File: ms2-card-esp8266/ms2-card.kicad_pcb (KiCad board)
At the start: 2 copper layers, 100 x 54 mm, 63 parts, among them J1 Schaltregler, J10 MicroSD_SPI_CD, J11 Conn_01x06, J2 ESP Prog, J20 Smartcard Connector, J21 PogoPin, J22 Card Edge, J23 Conn_01x04, J30 USB_B_Micro, J31 Power Select, J32 Conn_01x03, Q1 MMBT3904, Q2 MMBT3904, Q3 MMBT5401, SW1 RESET, U1 ESP-12F, U10 W25Q128JM, U2 FM24C64B, U20 BL1551B, U3 BL1551B, U30 CP2102N-A02-GQFN24R, U4 BL1551B, U6 AMS1117-3.3

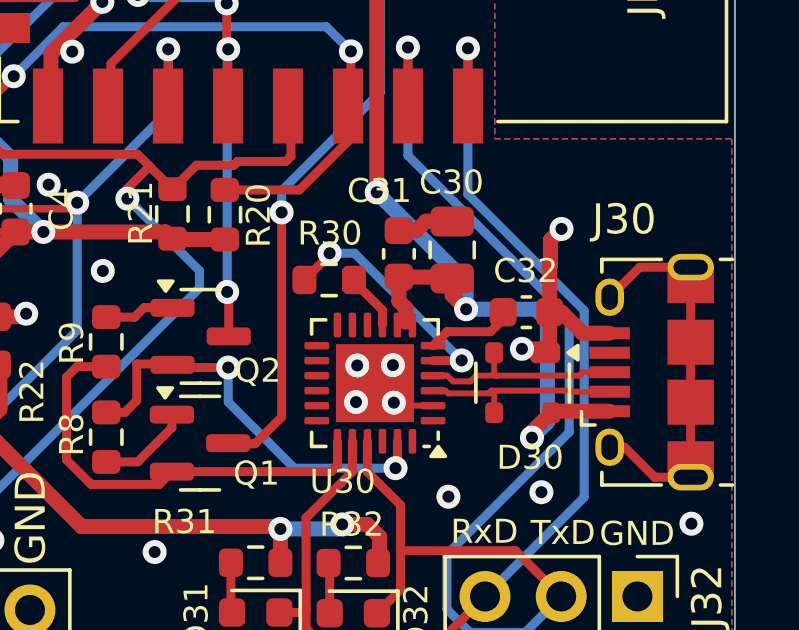
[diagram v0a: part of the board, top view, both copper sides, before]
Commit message: fix USB D+/D- swap
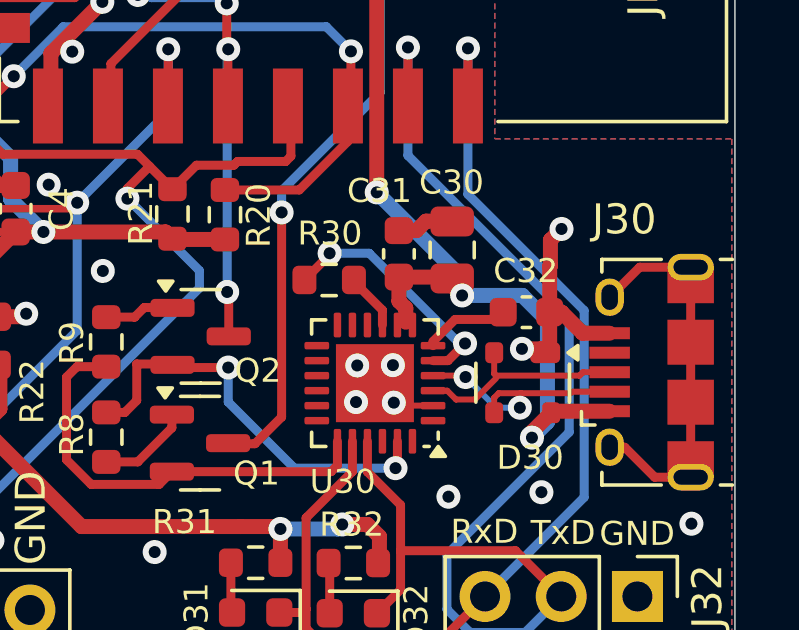
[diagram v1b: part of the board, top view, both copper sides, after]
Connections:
- D30 pad 2: /D- -> /D+
- D30 pad 3: /D+ -> /D-
- J30 pad 2: /D+ -> /D-
- J30 pad 3: /D- -> /D+
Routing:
- net /D-: track 6.89 -> 8.26 mm, vias 0 -> 2
- net /VBUS: track 70.7 -> 70.0 mm

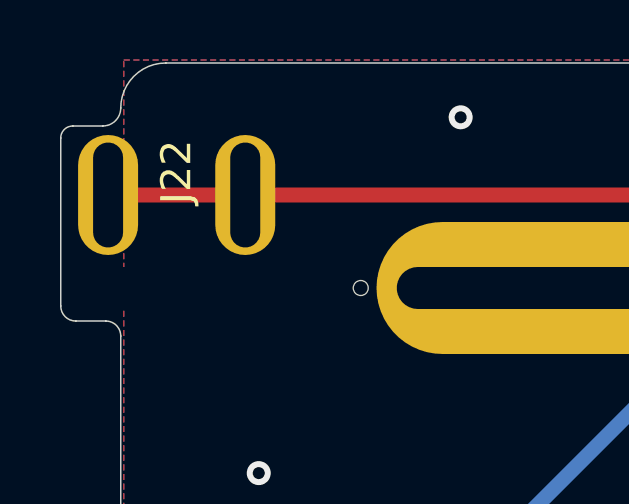
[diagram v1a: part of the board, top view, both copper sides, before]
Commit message: move edge connector a little bit
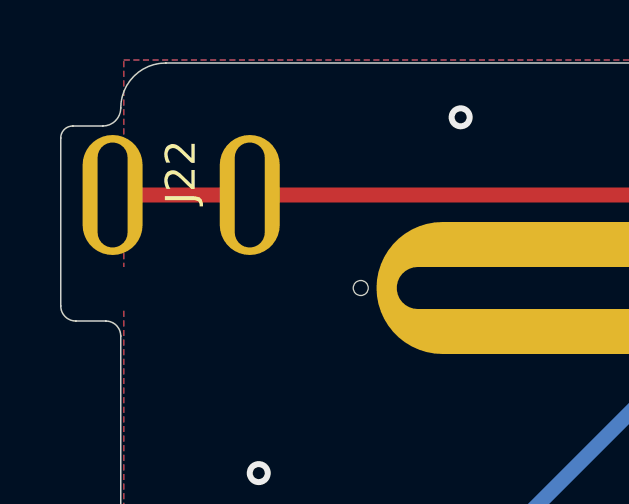
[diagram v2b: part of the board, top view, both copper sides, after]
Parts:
- moved J22 0.15 mm to (104.3, 104.4)
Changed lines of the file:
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@@
   )
   (footprint "MS2-Card:MS2_Edge" (layer "F.Cu")
-    (at 104.15 104.4 90)
+    (at 104.3 104.4 90)
     (property "Sheetfile" "ms2-card.kicad_sch")
     (property "Sheetname" "")

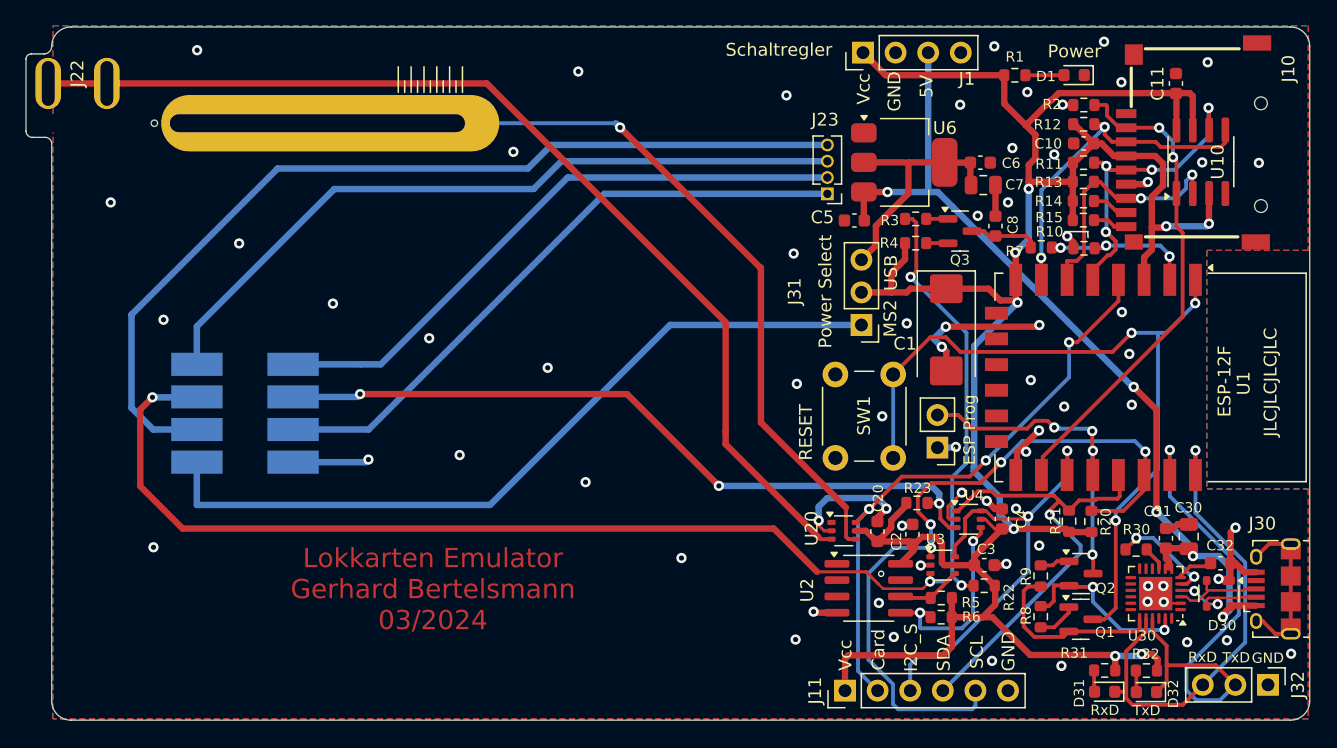
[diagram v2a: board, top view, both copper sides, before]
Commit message: make power LED a little bit less brighter
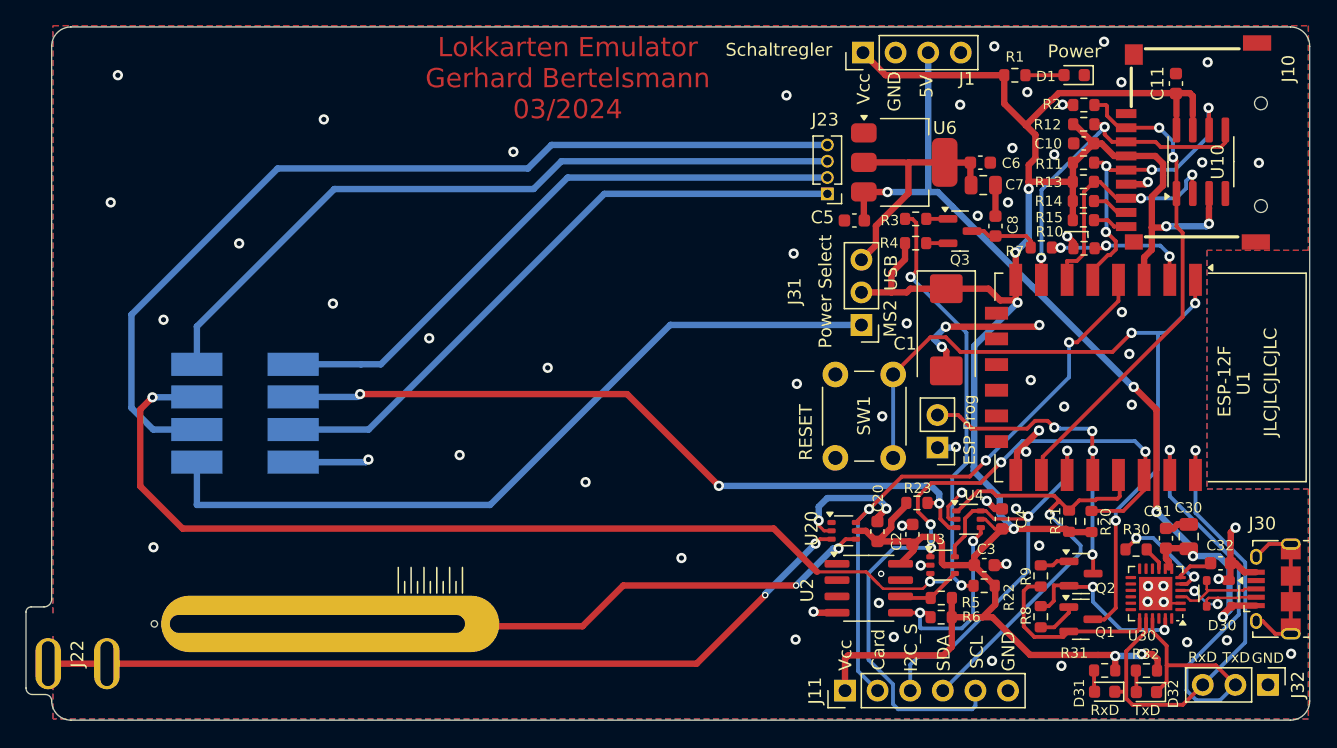
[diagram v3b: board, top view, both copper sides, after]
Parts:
- R1: value 330 -> 470
- moved J22 45.2 mm to (104.3, 149.6)
- moved J21 39.0 mm to (122.7, 146.5)
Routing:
- net /PP: track 63.8 -> 44.9 mm, vias 1 -> 2
- net Net-(J22-Pin_1): track 82.2 -> 65.1 mm, vias 0 -> 2
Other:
- outline, holes or cut-outs redrawn

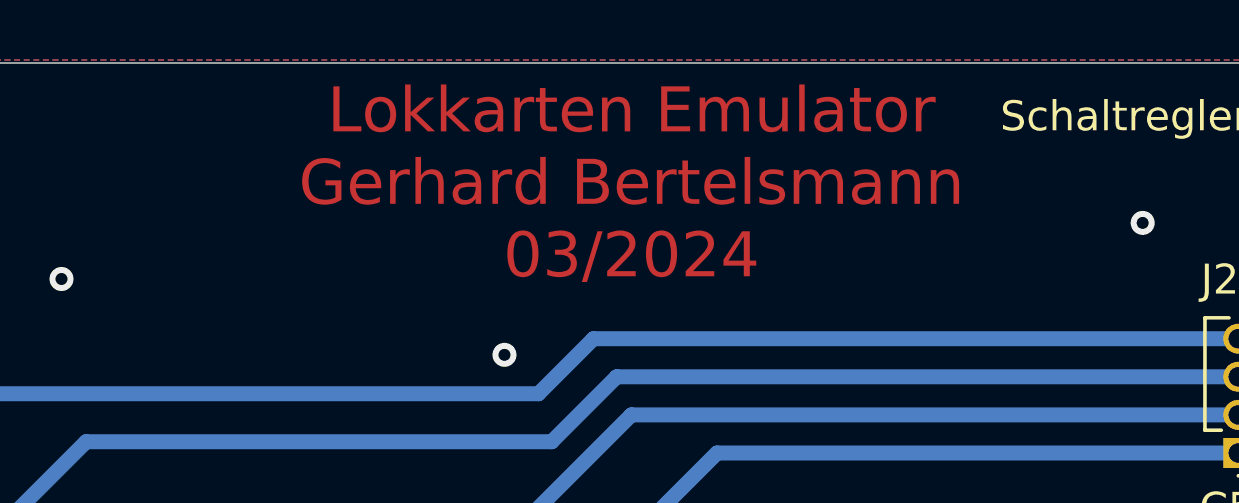
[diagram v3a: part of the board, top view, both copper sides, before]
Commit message: make power LED less brighter
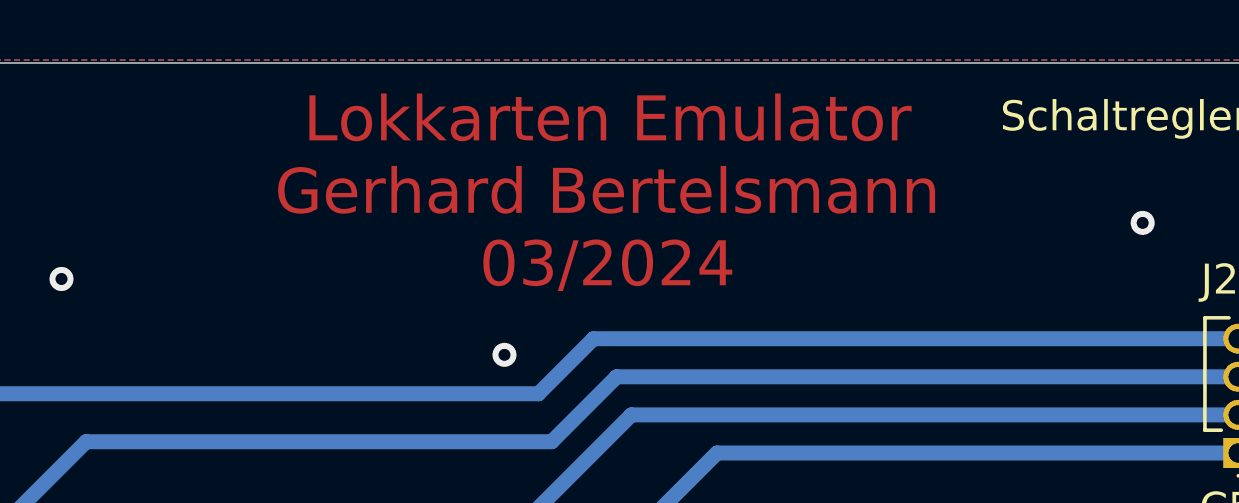
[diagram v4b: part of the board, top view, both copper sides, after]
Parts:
- R1: value 470 -> 680
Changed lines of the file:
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@@
   (title_block
     (title "Lokkkarten Emulator")
-    (date "2024-03-14")
-    (rev "0.995")
+    (date "2024-03-17")
+    (rev "0.996")
     (comment 1 "Gerhard Bertelsmann")
   )
@@
     (descr "Resistor SMD 0603 (1608 Metric), square (rectangular) end terminal, IPC_7351 nominal, (Body size source: IPC-SM-782 page 72, https://www.pcb-3d.com/wordpress/wp-content/uploads/ipc-sm-782a_amendment_1_and_2.pdf), generated with kicad-footprint-generator")
     (tags "resistor")
-    (property "LCSC" "C23179")
+    (property "LCSC" "C23228")
     (property "Sheetfile" "ms2-card.kicad_sch")
     (property "Sheetname" "")
@@
         (effects (font (size 0.8 0.8) (thickness 0.15)))
     )
-    (fp_text value "470" (at 0 1.43) (layer "F.Fab") hide
+    (fp_text value "680" (at 0 1.43) (layer "F.Fab") hide
         (effects (font (size 1 1) (thickness 0.15)))
     )
@@
   (gr_arc (start 196.5 100) (mid 197.56066 100.43934) (end 198 101.5)
     (stroke (width 0.05) (type solid)) (layer "Edge.Cuts"))
-  (gr_text "Lokkarten Emulator\nGerhard Bertelsmann\n03/2024" (at 140.2 104) (layer "F.Cu")
+  (gr_text "Lokkarten Emulator\nGerhard Bertelsmann\n03/2024" (at 139.4 104.3) (layer "F.Cu")
     (effects (font (size 1.5 1.5) (thickness 0.3)))
   )

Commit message: fix markings
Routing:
- net /VBUS: track 70.0 -> 71.1 mm

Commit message: update to KiCad 7.0 - wip
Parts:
- U2: value FM24C64B -> FM24CL64B
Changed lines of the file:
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@@
   (title_block
     (title "Lokkkarten Emulator")
-    (date "2024-03-17")
+    (date "2024-03-18")
     (rev "0.996")
     (comment 1 "Gerhard Bertelsmann")
@@
         (effects (font (size 1 1) (thickness 0.15)))
     )
-    (fp_text value "FM24C64B" (at -4.75 0.5 90) (layer "F.Fab") hide
+    (fp_text value "FM24CL64B" (at -4.75 0.5 90) (layer "F.Fab") hide
         (effects (font (size 0.8 0.8) (thickness 0.15)))
     )
